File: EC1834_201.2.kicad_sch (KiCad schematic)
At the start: 69 parts, among them X4 Lautsprecher, X7 DB9_Female

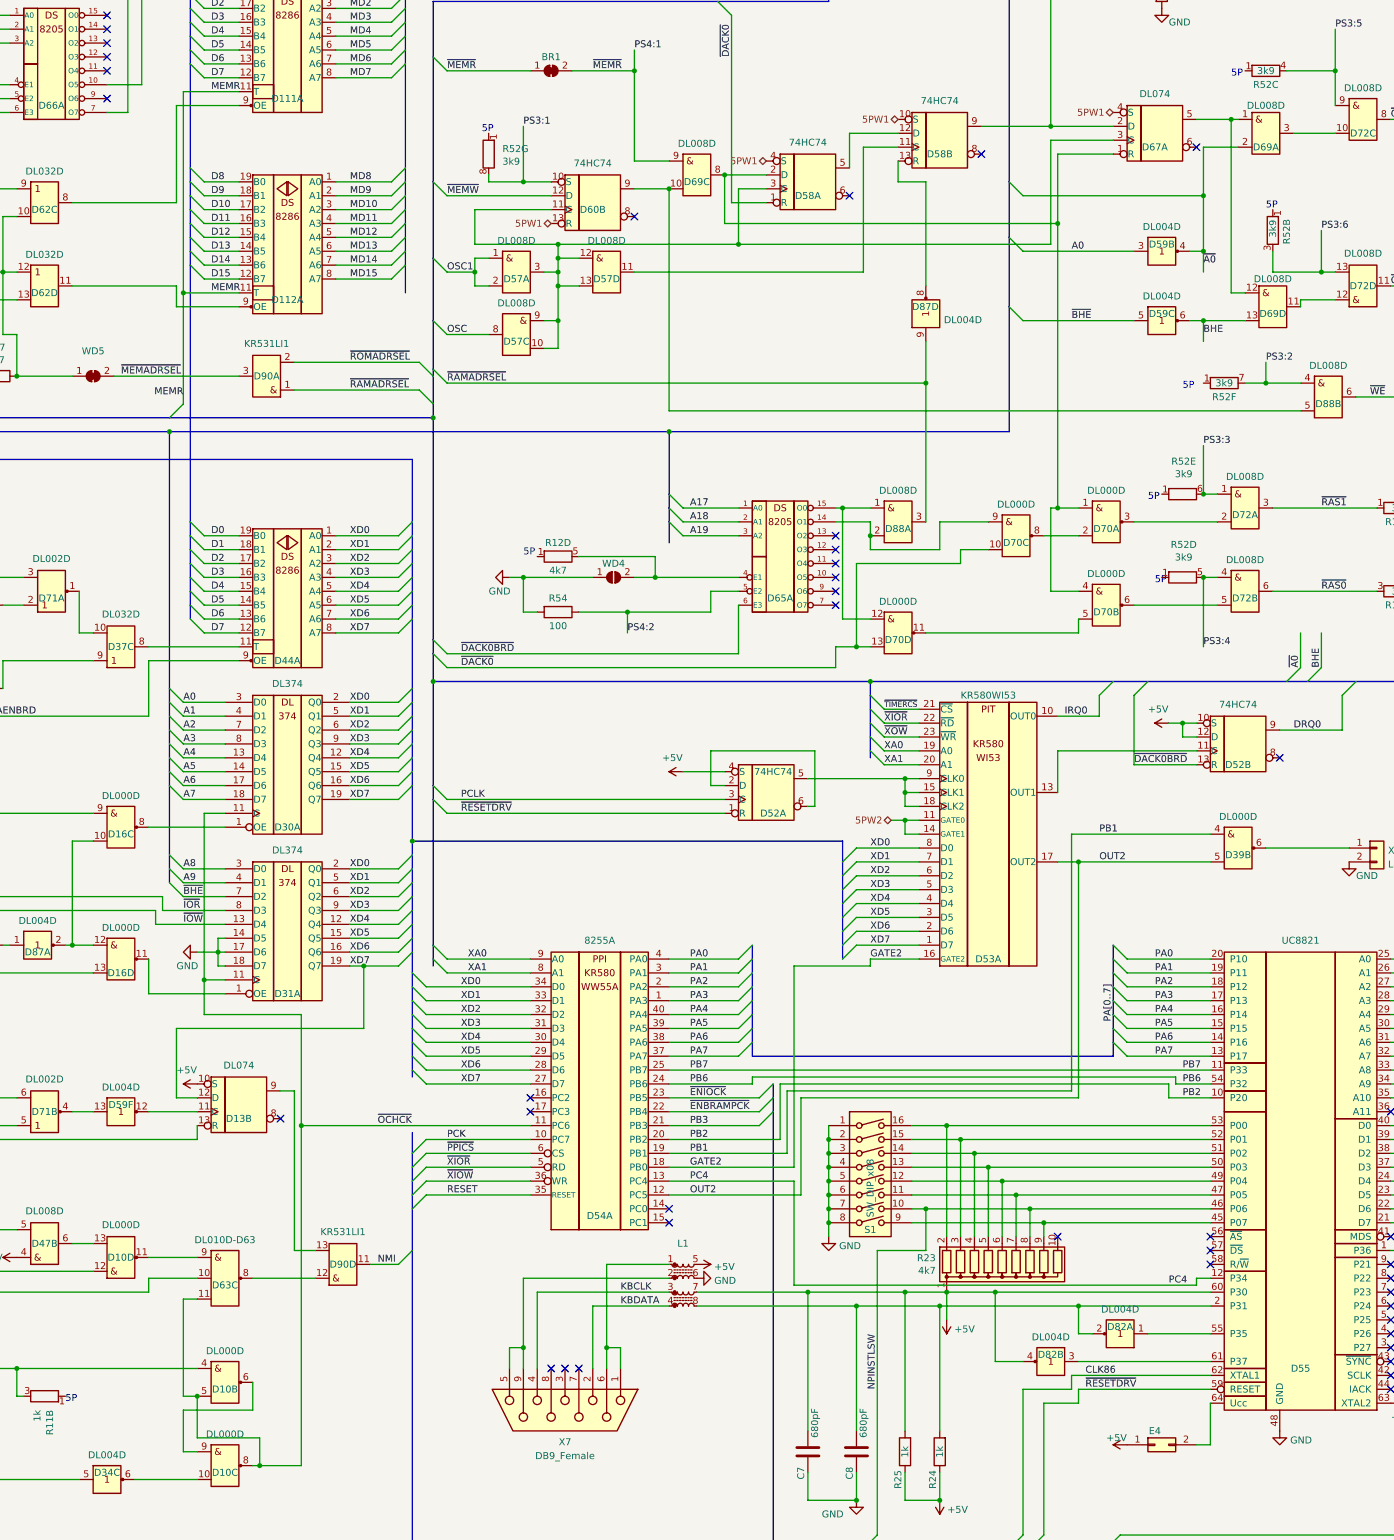
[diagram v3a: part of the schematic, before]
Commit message: Fixed wrong symbol (some DL008 are 74S00)
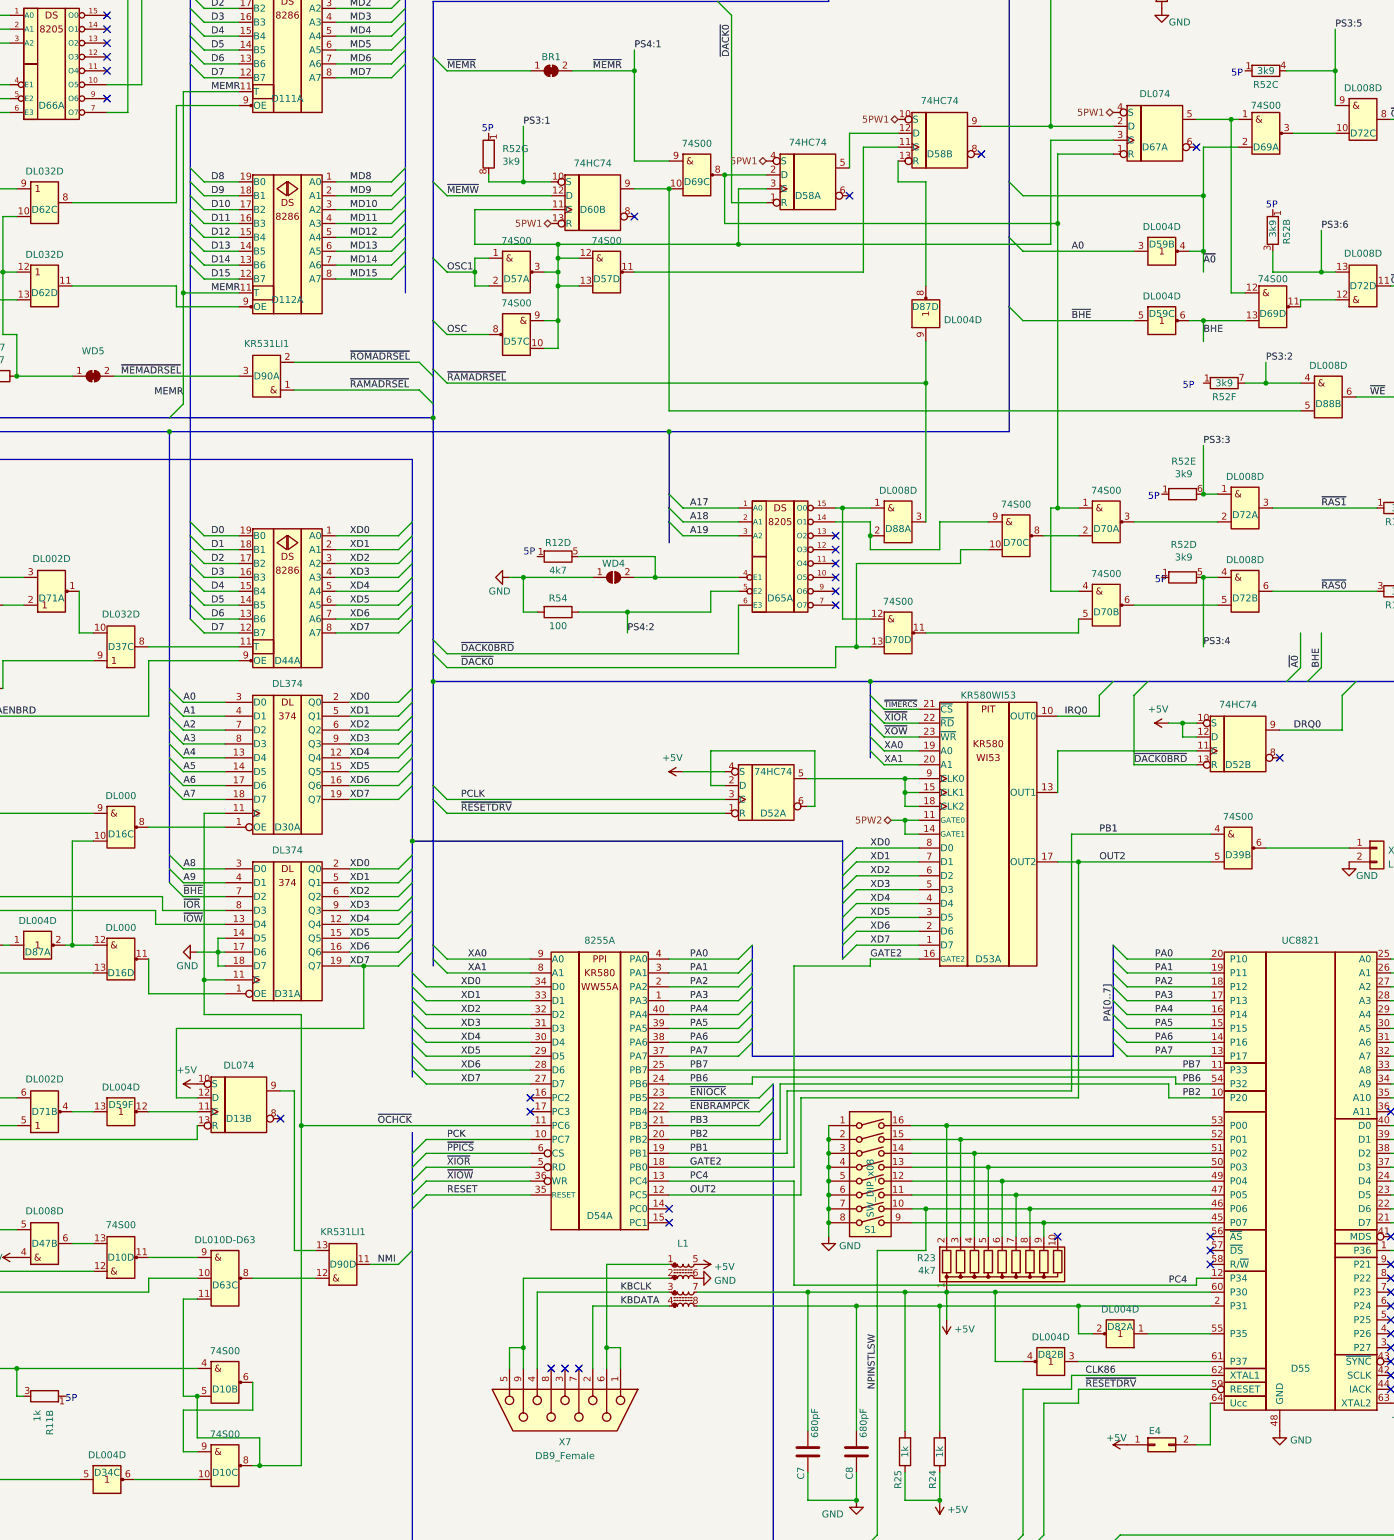
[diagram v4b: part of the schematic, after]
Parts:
- D10, D39, D70: value DL000D -> 74S00
- D16: value DL000D -> DL000
- D57, D69: value DL008D -> 74S00; symbol RFT_Digitalschaltkreise:DL008D -> robotron_ec1834:DL000D

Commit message: Modifications to pass most ERC checks modified symbols for ERC check Added some notes
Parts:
- D5: symbol RFT_Digitalschaltkreise:DL030D -> robotron_ec1834:DL030D
- WD5: symbol Jumper:SolderJumper_2_Bridged -> Jumper:SolderJumper_2_Open
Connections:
- net ~{XOW} is gone; now on net ~{XIOW}: D53.23 (~{WR})
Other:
- note added: "entfällt auf 1834M!"
- note added: "offen!"
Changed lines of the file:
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@@
     (stroke (width 0) (type default) (color 0 0 0 0))
   )
+  (polyline (pts (xy 326.39 194.31) (xy 337.82 194.31))
+    (stroke (width 0.5) (type default) (color 132 0 132 1))
+  )
   (wire (pts (xy 149.86 49.53) (xy 165.1 49.53))
     (stroke (width 0) (type default) (color 0 0 0 0))
@@
     (stroke (width 0) (type default) (color 0 0 0 0))
   )
+  (polyline (pts (xy 326.39 194.31) (xy 326.39 223.52))
+    (stroke (width 0.5) (type default) (color 132 0 132 1))
+  )
   (bus (pts (xy 134.62 189.23) (xy 134.62 236.22))
     (stroke (width 0.5) (type default) (color 0 0 0 0))
@@
     (stroke (width 0) (type default) (color 0 0 0 0))
   )
+  (polyline (pts (xy 358.14 124.46) (xy 358.14 168.91))
+    (stroke (width 0.5) (type default) (color 132 0 132 1))
+  )
   (wire (pts (xy 341.63 226.06) (xy 341.63 232.41))
     (stroke (width 0) (type default) (color 0 0 0 0))
@@
     (stroke (width 0.5) (type default) (color 0 0 0 0))
   )
+  (polyline (pts (xy 337.82 223.52) (xy 337.82 194.31))
+    (stroke (width 0.5) (type default) (color 132 0 132 1))
+  )
   (wire (pts (xy 311.15 220.98) (xy 326.39 220.98))
     (stroke (width 0) (type default) (color 0 0 0 0))
@@
     (stroke (width 0.5) (type default) (color 0 0 0 0))
   )
+  (polyline (pts (xy 326.39 223.52) (xy 337.82 223.52))
+    (stroke (width 0.5) (type default) (color 132 0 132 1))
+  )
   (bus (pts (xy 179.07 284.48) (xy 179.07 288.29))
     (stroke (width 0.5) (type default) (color 0 0 0 0))
@@
     (stroke (width 0) (type default) (color 0 0 0 0))
   )
+  (polyline (pts (xy 358.14 168.91) (xy 346.71 168.91))
+    (stroke (width 0.5) (type default) (color 132 0 132 1))
+  )
   (wire (pts (xy 48.26 62.23) (xy 58.42 62.23))
     (stroke (width 0) (type default) (color 0 0 0 0))
@@
     (stroke (width 0.5) (type default) (color 0 0 0 0))
   )
+  (polyline (pts (xy 346.71 124.46) (xy 346.71 168.91))
+    (stroke (width 0.5) (type default) (color 132 0 132 1))
+  )
   (bus (pts (xy 85.09 157.48) (xy 85.09 186.69))
     (stroke (width 2) (type default) (color 0 0 0 0))
@@
     (stroke (width 0) (type default) (color 0 0 0 0))
   )
+  (polyline (pts (xy 346.71 124.46) (xy 358.14 124.46))
+    (stroke (width 0.5) (type default) (color 132 0 132 1))
+  )
   (bus (pts (xy 179.07 266.7) (xy 179.07 269.24))
     (stroke (width 0.5) (type default) (color 0 0 0 0))
@@
     (effects (font (size 1.27 1.27)) (justify left bottom))
   )
+  (text "offen!" (at 118.11 184.15 0)
+    (effects (font (size 1.27 1.27) (thickness 0.254) bold) (justify left bottom))
+  )
+  (text "entfällt \nauf 1834M!" (at 326.39 210.82 0)
+    (effects (font (size 1.27 1.27)) (justify left bottom))
+  )
   (text "5P" (at 314.96 217.17 0)
     (effects (font (size 1.27 1.27)) (justify left bottom))
@@
     (effects (font (size 1.27 1.27)) (justify left bottom))
   )
+  (text "offen!" (at 213.36 219.71 0)
+    (effects (font (size 1.27 1.27) (thickness 0.254) bold) (justify left bottom))
+  )
+  (text "entfällt \nauf 1834M!" (at 346.71 146.05 0)
+    (effects (font (size 1.27 1.27)) (justify left bottom))
+  )
   (text "5P" (at 115.57 367.03 0)
     (effects (font (size 1.27 1.27)) (justify left bottom))
@@
     (effects (font (size 1.27 1.27)) (justify left bottom))
   )
-  (label "~{XOW}" (at 265.43 245.11 0)
+  (label "~{XIOW}" (at 265.43 245.11 0)
     (effects (font (size 1.27 1.27)) (justify left bottom))
   )
@@
     (effects (font (size 1.27 1.27)) (justify left bottom))
   )
-  (label "PS3:6" (at 345.44 152.4 0)
-    (effects (font (size 1.27 1.27)) (justify left bottom))
+  (label "PS3:6" (at 345.44 152.4 180)
+    (effects (font (size 1.27 1.27)) (justify right bottom))
   )
   (label "MEM6" (at 374.65 85.09 0)
@@
     (effects (font (size 1.27 1.27)) (justify left bottom))
   )
-  (hierarchical_label "{AENBRD ~{AEN} MEMR PB3 ~{IOCHCK} BHE DRQ0 ~{DACK0BRD} DACK0 ~{DACK0} ~{INTA} ~{IOR} ~{IOW} ~{XIOR} ~{XIOW} ~{XMEMR} ~{MEMR} ~{MEMW} ~{NMIADRCS} ~{TIMERCS} ~{PPICS} ~{NIMREGCS} IRQ0 IRQ1 OSC OSC1 PCLK CLK86 ~{MEMADRSEL} NMI NPNPI RESET ~{RESETDRV} MDPEE MDPOE}" (shape input)
+  (hierarchical_label "{~{A0} AEN AENBRD AENBRDW AENDMA ALE BHE BS-{slash}WAIT CLK CLK86 DACK0 DEN DT-{slash}R DRQ0 DRQ1 DRQ2 DRQ3 HOLDA HRQDMA IED INT IOCHRDY IORW IRQ0 IRQ1 IRQ2 IRQ3 IRQ4 IRQ5 IRQ6 IRQ7 IRQ8 IRQ10 IRQ11 IRQ12 IRQ14 IRQ15 MASTER MDPEE MDPOE MEMR NPNPI NMI PB3 PCLK OSC OSC1 QS0 QS1 RDY-{slash}WAIT READY RDYTODMA RESET RESETDRV TC VA0 XA0 ~{AEN} ~{BHE} ~{CLK} ~{DACK0BRD} ~{DACK0} ~{DACK1} ~{DACK2} ~{DACK3} ~{DMACS} ~{DMAAEN} ~{INTA} ~{INTRCS1} ~{INTRCS2} ~{IOR} ~{IOW} ~{GT1} ~{LOCK} ~{MASTER} ~{MEMADRSEL} ~{MEMCS16} ~{MEMR} ~{MEMW} ~{NMIADRCS} ~{NMIREGCS} ~{PPICS} ~{RESETDRV} ~{S0} ~{S1} ~{S2} ~{TIMERCS} ~{XIOR} ~{XIOW} ~{XMEMR} ~{XMEMW} ~{YIOR} ~{YIOW}}" (shape bidirectional)
     (at 21.59 396.24 0)
     (effects (font (size 1.27 1.27)) (justify left))
   )
-  (hierarchical_label "{A[0..19] VA0 ~{BHE}}" (shape input) (at 41.91 187.96 0)
+  (hierarchical_label "{A[0..19] VA0 ~{BHE}}" (shape bidirectional) (at 41.91 187.96 0)
     (effects (font (size 1.27 1.27)) (justify left))
   )
@@
     (effects (font (size 1.27 1.27)) (justify right))
   )
-  (hierarchical_label "D[0..15]" (shape input) (at 24.13 93.98 0)
+  (hierarchical_label "D[0..15]" (shape bidirectional) (at 24.13 93.98 0)
     (effects (font (size 1.27 1.27)) (justify left))
   )
-  (hierarchical_label "MD[0..15]" (shape input) (at 464.82 24.13 0)
+  (hierarchical_label "MD[0..15]" (shape bidirectional) (at 464.82 24.13 0)
     (effects (font (size 1.27 1.27)) (justify left))
   )
@@
     (effects (font (size 1.27 1.27)) (justify right))
   )
-  (hierarchical_label "{MEM[0..8] ~{RAS0} ~{RAS1} ~{CASL} ~{CASH} ~{WE}}" (shape input) (at 464.82 38.1 0)
+  (hierarchical_label "{MEM[0..8] ~{RAS0} ~{RAS1} ~{CASL} ~{CASH} ~{WE}}" (shape bidirectional) (at 464.82 38.1 0)
     (effects (font (size 1.27 1.27)) (justify left))
   )
-  (hierarchical_label "XA[0..19]" (shape input) (at 24.13 81.28 0)
+  (hierarchical_label "XA[0..19]" (shape bidirectional) (at 24.13 81.28 0)
     (effects (font (size 1.27 1.27)) (justify left))
   )
-  (hierarchical_label "XD[0..15]" (shape input) (at 41.91 195.58 0)
+  (hierarchical_label "XD[0..15]" (shape bidirectional) (at 41.91 195.58 0)
     (effects (font (size 1.27 1.27)) (justify left))
   )
@@
     (effects (font (size 1.27 1.27)) (justify right))
   )
-  (symbol (lib_id "robotron_ec1834:U2764") (at 67.31 62.23 0) (unit 1)
+  (symbol (lib_name "U2764_1") (lib_id "robotron_ec1834:U2764") (at 67.31 62.23 0) (unit 1)
     (in_bom yes) (on_board yes)
     (property "Reference" "D101" (id 0) (at 67.31 81.28 0))
@@
     (pin "9")
     (pin "14")
-    (pin "26")
     (pin "28")
   )
-  (symbol (lib_id "robotron_ec1834:U2764") (at 113.03 62.23 0) (unit 1)
+  (symbol (lib_name "U2764_2") (lib_id "robotron_ec1834:U2764") (at 113.03 62.23 0) (unit 1)
     (in_bom yes) (on_board yes)
     (property "Reference" "D116" (id 0) (at 113.03 81.28 0))
@@
     (pin "9")
     (pin "14")
-    (pin "26")
     (pin "28")
   )
-  (symbol (lib_id "robotron_ec1834:U2764") (at 173.99 62.23 0) (unit 1)
+  (symbol (lib_name "U2764_3") (lib_id "robotron_ec1834:U2764") (at 173.99 62.23 0) (unit 1)
     (in_bom yes) (on_board yes)
     (property "Reference" "D115" (id 0) (at 173.99 81.28 0))
@@
     (pin "9")
     (pin "14")
-    (pin "26")
     (pin "28")
   )
@@
     (pin "9")
     (pin "14")
-    (pin "26")
     (pin "28")
   )
@@
     (pin "8")
   )
-  (symbol (lib_id "RFT_Digitalschaltkreise:DL030D") (at 71.12 125.73 0) (unit 1)
+  (symbol (lib_id "robotron_ec1834:DL030D") (at 71.12 125.73 0) (unit 1)
     (in_bom yes) (on_board yes)
     (property "Reference" "D5" (id 0) (at 71.12 132.08 0))
@@
       (effects (font (size 1.27 1.27)) hide)
     )
-    (pin "10")
     (pin "8")
     (pin "1")
+    (pin "10")
     (pin "11")
     (pin "12")
@@
     (pin "7")
   )
-  (symbol (lib_name "DS8205_1") (lib_id "robotron_ec1834:DS8205") (at 246.38 212.09 0) (unit 1)
+  (symbol (lib_id "robotron_ec1834:DS8205") (at 246.38 212.09 0) (unit 1)
     (in_bom yes) (on_board yes)
     (property "Reference" "D65" (id 0) (at 246.38 219.71 0))
@@
   (symbol (lib_id "Device:R_Network07_Split") (at 336.55 152.4 0) (unit 2)
     (in_bom yes) (on_board yes)
-    (property "Reference" "R52" (id 0) (at 339.09 154.94 90)
+    (property "Reference" "R52" (id 0) (at 334.01 154.94 90)
       (effects (font (size 1.27 1.27)) (justify left))
     )
@@
     (pin "1")
   )
-  (symbol (lib_id "Jumper:SolderJumper_2_Bridged") (at 120.65 179.07 0) (unit 1)
+  (symbol (lib_id "Jumper:SolderJumper_2_Open") (at 120.65 179.07 0) (unit 1)
     (in_bom yes) (on_board yes) (fields_autoplaced)
     (property "Reference" "WD5" (id 0) (at 120.65 174.4812 0))

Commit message: Added some notes to schematics
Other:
- note added: "BIOS Erweiterung F8000-FBFFF"
- note added: "BIOS FC000-FFFFF"
- note added: "NMI Maskierung"
- note added: "NMI Maskierung via Port A0h 80h NMI erlaubt 00h NMI verboten"
- note added: "Parity Behandlung"
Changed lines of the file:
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@@
     (stroke (width 0.5) (type default) (color 0 0 0 0))
+  )
+  (polyline (pts (xy 86.36 321.31) (xy 162.56 321.31))
+    (stroke (width 0) (type default) (color 0 0 0 0))
   )
   (wire (pts (xy 262.89 205.74) (xy 262.89 208.28))
@@
     (stroke (width 0) (type default) (color 0 0 0 0))
   )
+  (polyline (pts (xy 132.08 302.26) (xy 162.56 302.26))
+    (stroke (width 0) (type default) (color 0 0 0 0))
+  )
   (wire (pts (xy 57.15 88.9) (xy 102.87 88.9))
     (stroke (width 0) (type default) (color 0 0 0 0))
@@
   )
   (wire (pts (xy 284.48 205.74) (xy 275.59 205.74))
+    (stroke (width 0) (type default) (color 0 0 0 0))
+  )
+  (polyline (pts (xy 132.08 250.19) (xy 132.08 302.26))
     (stroke (width 0) (type default) (color 0 0 0 0))
   )
@@
     (stroke (width 0) (type default) (color 0 0 0 0))
   )
+  (polyline (pts (xy 86.36 384.81) (xy 154.94 384.81))
+    (stroke (width 0) (type default) (color 0 0 0 0))
+  )
   (wire (pts (xy 255.27 334.01) (xy 255.27 336.55))
     (stroke (width 0) (type default) (color 0 0 0 0))
@@
   (bus (pts (xy 133.35 59.69) (xy 133.35 62.23))
     (stroke (width 0.5) (type default) (color 0 0 0 0))
+  )
+  (polyline (pts (xy 86.36 250.19) (xy 132.08 250.19))
+    (stroke (width 0) (type default) (color 0 0 0 0))
   )
   (bus (pts (xy 382.27 54.61) (xy 382.27 77.47))
@@
     (stroke (width 0) (type default) (color 0 0 0 0))
   )
+  (polyline (pts (xy 162.56 302.26) (xy 162.56 321.31))
+    (stroke (width 0) (type default) (color 0 0 0 0))
+  )
   (wire (pts (xy 228.6 41.91) (xy 238.76 41.91))
     (stroke (width 0) (type default) (color 0 0 0 0))
@@
     (stroke (width 0) (type default) (color 0 0 0 0))
   )
+  (polyline (pts (xy 154.94 370.84) (xy 154.94 384.81))
+    (stroke (width 0) (type default) (color 0 0 0 0))
+  )
   (wire (pts (xy 256.54 74.93) (xy 261.62 74.93))
     (stroke (width 0) (type default) (color 0 0 0 0))
@@
     (stroke (width 0) (type default) (color 0 0 0 0))
   )
+  (polyline (pts (xy 86.36 370.84) (xy 154.94 370.84))
+    (stroke (width 0) (type default) (color 0 0 0 0))
+  )
   (wire (pts (xy 48.26 67.31) (xy 58.42 67.31))
     (stroke (width 0) (type default) (color 0 0 0 0))
@@
   (wire (pts (xy 170.18 287.02) (xy 176.53 287.02))
     (stroke (width 0) (type default) (color 0 0 0 0))
+  )
+  (text "NMI Maskierung" (at 88.9 373.38 0)
+    (effects (font (size 1.27 1.27)) (justify left bottom))
   )
   (text "5P" (at 335.28 148.59 0)
     (effects (font (size 1.27 1.27)) (justify left bottom))
   )
+  (text "NMI Maskierung\n\nvia Port A0h \n80h NMI erlaubt\n00h NMI verboten"
+    (at 96.52 256.54 0)
+    (effects (font (size 1.27 1.27)) (justify left bottom))
+  )
   (text "5P" (at 320.04 181.61 0)
     (effects (font (size 1.27 1.27)) (justify left bottom))
   )
+  (text "BIOS\nFC000-FFFFF" (at 60.96 35.56 0)
+    (effects (font (size 1.27 1.27)) (justify left bottom))
+  )
   (text "5P" (at 90.17 330.2 0)
     (effects (font (size 1.27 1.27)) (justify left bottom))
@@
     (effects (font (size 1.27 1.27)) (justify left bottom))
   )
+  (text "BIOS\nFC000-FFFFF" (at 106.68 35.56 0)
+    (effects (font (size 1.27 1.27)) (justify left bottom))
+  )
   (text "5P" (at 314.96 217.17 0)
     (effects (font (size 1.27 1.27)) (justify left bottom))
@@
     (effects (font (size 1.27 1.27)) (justify left bottom))
   )
+  (text "Parity Behandlung" (at 95.25 353.06 0)
+    (effects (font (size 1.27 1.27)) (justify left bottom))
+  )
   (text "5P" (at 191.77 134.62 0)
     (effects (font (size 1.27 1.27)) (justify left bottom))
   )
+  (text "BIOS Erweiterung\nF8000-FBFFF" (at 166.37 35.56 0)
+    (effects (font (size 1.27 1.27)) (justify left bottom))
+  )
   (text "offen!" (at 213.36 219.71 0)
     (effects (font (size 1.27 1.27) (thickness 0.254) bold) (justify left bottom))
@@
     (effects (font (size 1.27 1.27)) (justify left bottom))
   )
+  (text "BIOS Erweiterung\nF8000-FBFFF" (at 240.03 35.56 0)
+    (effects (font (size 1.27 1.27)) (justify left bottom))
+  )
